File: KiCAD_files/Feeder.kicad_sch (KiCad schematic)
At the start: 82 parts, among them J405 Conn_01x02_Male, J406 Conn_01x02_Male, J501 Conn_01x03, Q501 60V N channel, Q502 TK13P25D,RQ, T501 PA2467NL, U407 OPA316, U501 NCP12700, U503 TL431MFDT,215, U505 MCP1799T-5002H/DB

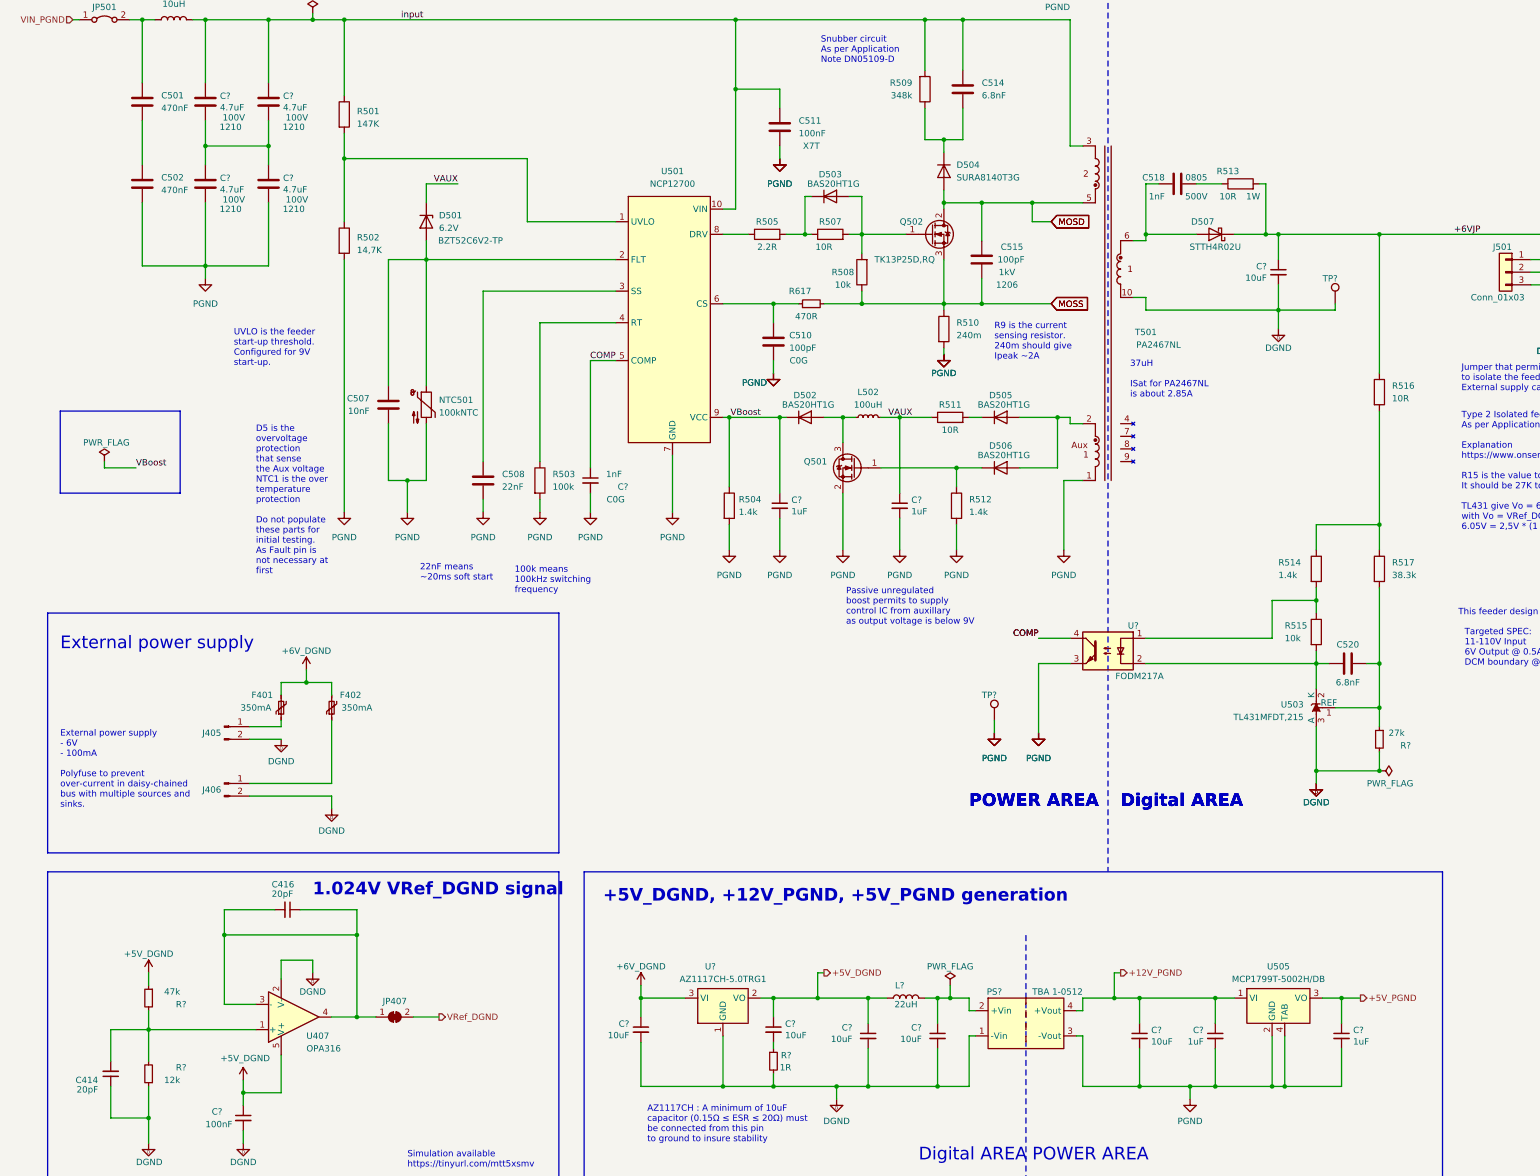
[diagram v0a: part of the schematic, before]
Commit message: Added netclasses and ERC rules for isolation clearances
Signed-off-by: Jean Alinei <jean.alinei@laas.fr>
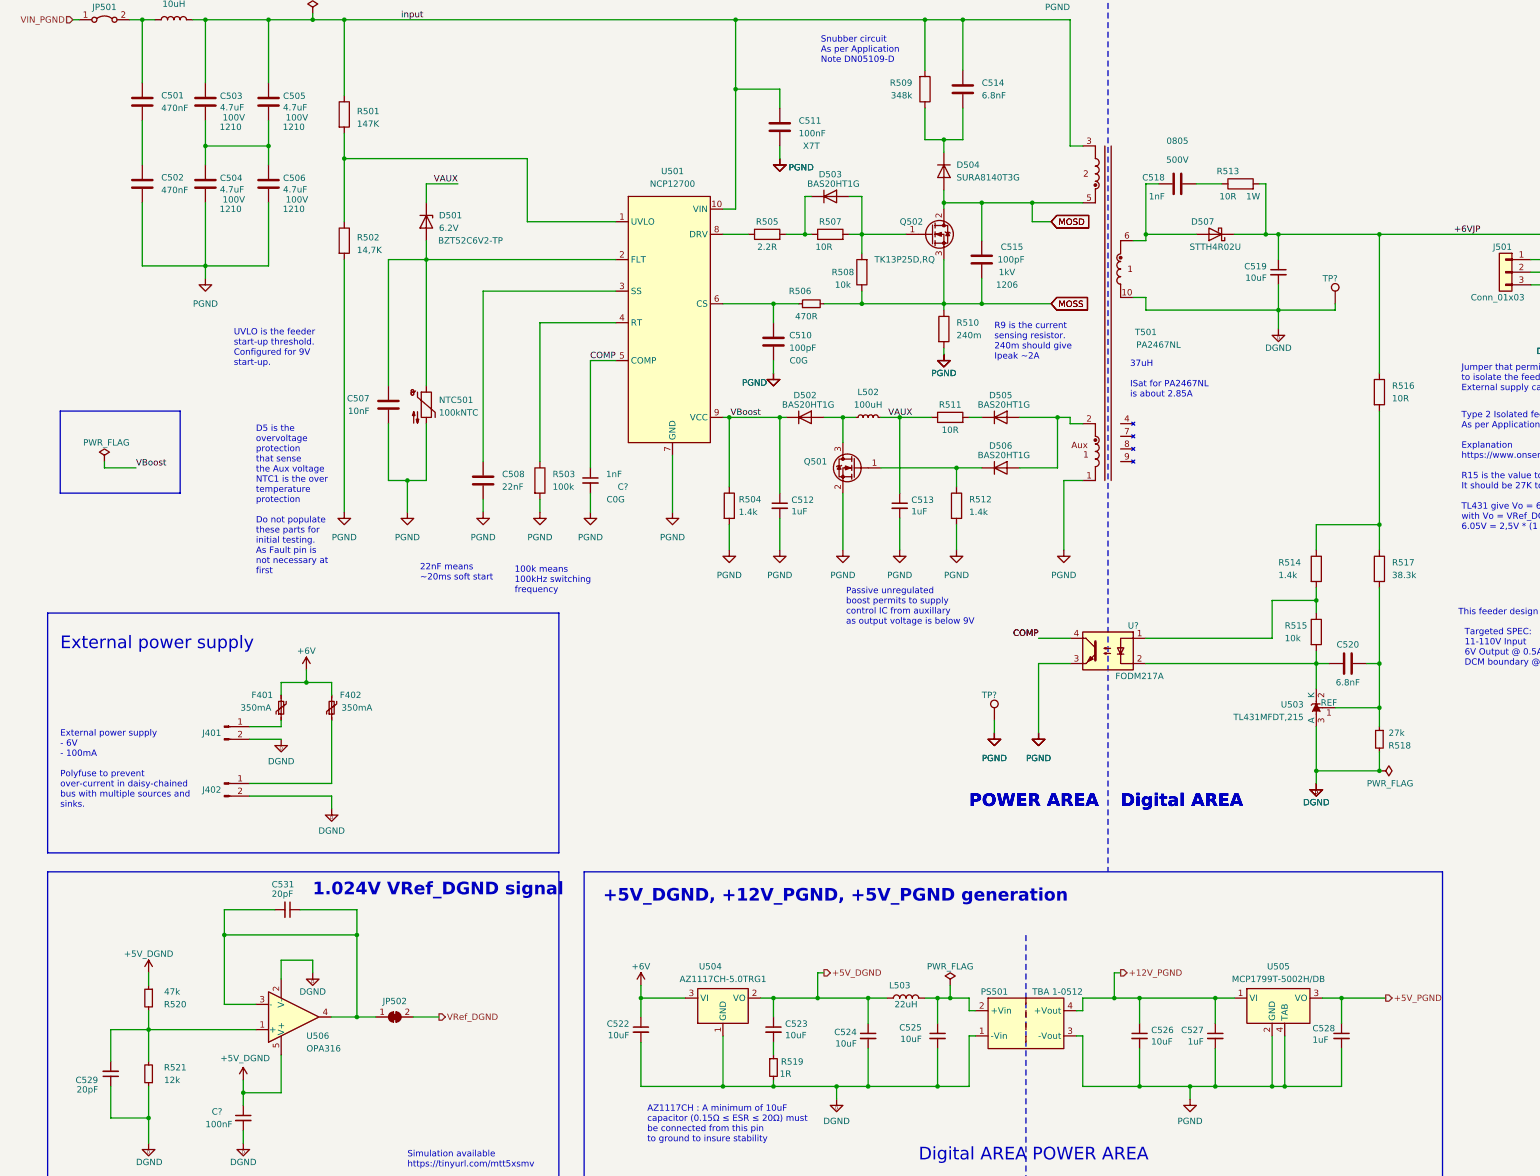
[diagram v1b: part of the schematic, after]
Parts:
- gave numbers to parts that had none: 21
- renumbered C414 to C529, C416 to C531, J405 to J401, J406 to J402, JP407 to JP502, R617 to R506, U407 to U506
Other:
- moved on the sheet: R519
